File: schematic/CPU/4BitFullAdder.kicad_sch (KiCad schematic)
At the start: 5 parts, among them U23 74LS86, U24 74LS08, U25 74LS86, U26 74LS08, U27 74LS32

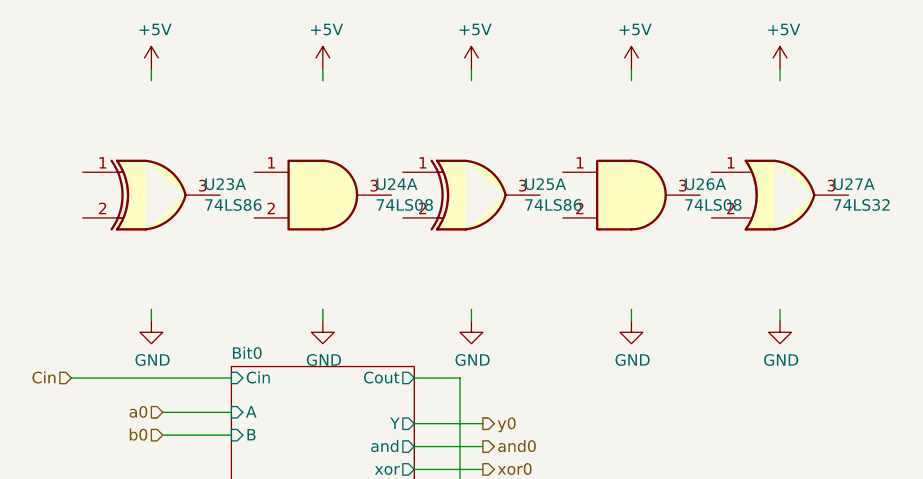
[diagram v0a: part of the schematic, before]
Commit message: ttl fpga: factorization works in sim and fpga
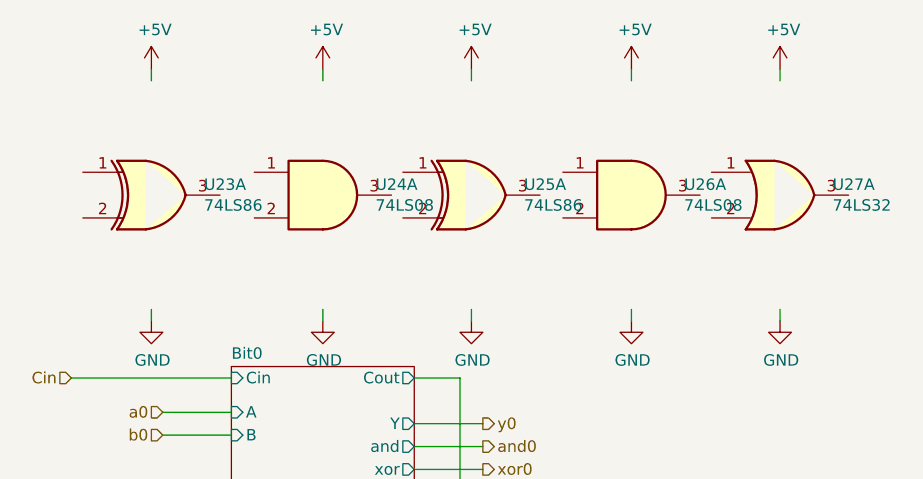
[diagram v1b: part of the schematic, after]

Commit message: io: async register + reversed bus
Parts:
- renumbered U23 to U28, U24 to U29, U25 to U30, U26 to U31, U27 to U32
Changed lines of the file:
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@@
   (symbol (lib_id "74xx:74LS86") (at 73.66 39.37 0)
     (in_bom yes) (on_board yes)
-    (property "Reference" "U23" (id 0) (at 79.502 38.2016 0)
+    (property "Reference" "U28" (id 0) (at 79.502 38.2016 0)
       (effects (font (size 1.27 1.27)) (justify left))
     )
@@
   (symbol (lib_id "74xx:74LS86") (at 109.22 39.37 0)
     (in_bom yes) (on_board yes)
-    (property "Reference" "U25" (id 0) (at 115.062 38.2016 0)
+    (property "Reference" "U30" (id 0) (at 115.062 38.2016 0)
       (effects (font (size 1.27 1.27)) (justify left))
     )
@@
   (symbol (lib_id "74xx:74LS08") (at 92.71 39.37 0)
     (in_bom yes) (on_board yes)
-    (property "Reference" "U24" (id 0) (at 98.552 38.2016 0)
+    (property "Reference" "U29" (id 0) (at 98.552 38.2016 0)
       (effects (font (size 1.27 1.27)) (justify left))
     )
@@
   (symbol (lib_id "74xx:74LS08") (at 127 39.37 0)
     (in_bom yes) (on_board yes)
-    (property "Reference" "U26" (id 0) (at 132.842 38.2016 0)
+    (property "Reference" "U31" (id 0) (at 132.842 38.2016 0)
       (effects (font (size 1.27 1.27)) (justify left))
     )
@@
   (symbol (lib_id "74xx:74LS32") (at 143.51 39.37 0)
     (in_bom yes) (on_board yes)
-    (property "Reference" "U27" (id 0) (at 149.352 38.2016 0)
+    (property "Reference" "U32" (id 0) (at 149.352 38.2016 0)
       (effects (font (size 1.27 1.27)) (justify left))
     )
@@
   (symbol (lib_id "power:+5V") (at 73.66 25.4 0)
     (in_bom yes) (on_board yes)
-    (property "Reference" "#PWR081" (id 0) (at 73.66 29.21 0)
+    (property "Reference" "#PWR091" (id 0) (at 73.66 29.21 0)
       (effects (font (size 1.27 1.27)) hide)
     )
@@
   (symbol (lib_id "power:+5V") (at 92.71 25.4 0)
     (in_bom yes) (on_board yes)
-    (property "Reference" "#PWR083" (id 0) (at 92.71 29.21 0)
+    (property "Reference" "#PWR093" (id 0) (at 92.71 29.21 0)
       (effects (font (size 1.27 1.27)) hide)
     )
@@
   (symbol (lib_id "power:+5V") (at 109.22 25.4 0)
     (in_bom yes) (on_board yes)
-    (property "Reference" "#PWR085" (id 0) (at 109.22 29.21 0)
+    (property "Reference" "#PWR095" (id 0) (at 109.22 29.21 0)
       (effects (font (size 1.27 1.27)) hide)
     )
@@
   (symbol (lib_id "power:GND") (at 143.51 53.34 0)
     (in_bom yes) (on_board yes)
-    (property "Reference" "#PWR090" (id 0) (at 143.51 59.69 0)
+    (property "Reference" "#PWR0100" (id 0) (at 143.51 59.69 0)
       (effects (font (size 1.27 1.27)) hide)
     )
@@
   (symbol (lib_id "power:GND") (at 127 53.34 0)
     (in_bom yes) (on_board yes)
-    (property "Reference" "#PWR088" (id 0) (at 127 59.69 0)
+    (property "Reference" "#PWR098" (id 0) (at 127 59.69 0)
       (effects (font (size 1.27 1.27)) hide)
     )
@@
   (symbol (lib_id "power:GND") (at 109.22 53.34 0)
     (in_bom yes) (on_board yes)
-    (property "Reference" "#PWR086" (id 0) (at 109.22 59.69 0)
+    (property "Reference" "#PWR096" (id 0) (at 109.22 59.69 0)
       (effects (font (size 1.27 1.27)) hide)
     )
@@
   (symbol (lib_id "power:GND") (at 92.71 53.34 0)
     (in_bom yes) (on_board yes)
-    (property "Reference" "#PWR084" (id 0) (at 92.71 59.69 0)
+    (property "Reference" "#PWR094" (id 0) (at 92.71 59.69 0)
       (effects (font (size 1.27 1.27)) hide)
     )
@@
   (symbol (lib_id "power:GND") (at 73.66 53.34 0)
     (in_bom yes) (on_board yes)
-    (property "Reference" "#PWR082" (id 0) (at 73.66 59.69 0)
+    (property "Reference" "#PWR092" (id 0) (at 73.66 59.69 0)
       (effects (font (size 1.27 1.27)) hide)
     )
@@
   (symbol (lib_id "power:+5V") (at 127 25.4 0)
     (in_bom yes) (on_board yes)
-    (property "Reference" "#PWR087" (id 0) (at 127 29.21 0)
+    (property "Reference" "#PWR097" (id 0) (at 127 29.21 0)
       (effects (font (size 1.27 1.27)) hide)
     )
@@
   (symbol (lib_id "power:+5V") (at 143.51 25.4 0)
     (in_bom yes) (on_board yes)
-    (property "Reference" "#PWR089" (id 0) (at 143.51 29.21 0)
-      (effects (font (size 1.27 1.27)) hide)
-    )
+    (property "Reference" "#PWR099" (id 0) (at 143.51 29.21 0)
+      (effects (font (size 1.27 1.27)) hide)
+    )

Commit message: alu figures, modules finished
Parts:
- U28, U30: value 74LS86 -> (none); footprint Package_DIP:DIP-14_W7.62mm -> (none)
- U29, U31: value 74LS08 -> (none); footprint Package_DIP:DIP-14_W7.62mm -> (none)
- U32: value 74LS32 -> (none); footprint Package_DIP:DIP-14_W7.62mm -> (none)
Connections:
- net +5V: now also U28.14 (VCC), U29.14 (VCC), U30.14 (VCC), U31.14 (VCC), U32.14 (VCC)
- net GND: now also U28.7 (GND), U29.7 (GND), U30.7 (GND), U31.7 (GND), U32.7 (GND)
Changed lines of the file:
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@@
     (effects (font (size 1.27 1.27)) (justify right))
   )
-  (symbol (lib_id "74xx:74LS86") (at 73.66 39.37 0)
+  (symbol (lib_id "74xx:74LS86") (at 73.66 39.37 0) (unit 5)
     (in_bom yes) (on_board yes)
     (property "Reference" "U28" (id 0) (at 79.502 38.2016 0)
       (effects (font (size 1.27 1.27)) (justify left))
     )
-    (property "Value" "74LS86" (id 1) (at 79.502 40.513 0)
-      (effects (font (size 1.27 1.27)) (justify left))
-    )
-    (property "Footprint" "Package_DIP:DIP-14_W7.62mm" (id 2) (at 73.66 39.37 0)
+    (property "Value" "" (id 1) (at 79.502 40.513 0)
+      (effects (font (size 1.27 1.27)) (justify left))
+    )
+    (property "Footprint" "" (id 2) (at 73.66 39.37 0)
       (effects (font (size 1.27 1.27)) hide)
     )
@@
       (effects (font (size 1.27 1.27)) hide)
     )
-    (pin "14")
-    (pin "7")
-  )
-  (symbol (lib_id "74xx:74LS86") (at 109.22 39.37 0)
+    (pin "1")
+    (pin "2")
+    (pin "3")
+    (pin "4")
+    (pin "5")
+    (pin "6")
+    (pin "10")
+    (pin "8")
+    (pin "9")
+    (pin "11")
+    (pin "12")
+    (pin "13")
+    (pin "14")
+    (pin "7")
+  )
+  (symbol (lib_id "74xx:74LS86") (at 109.22 39.37 0) (unit 5)
     (in_bom yes) (on_board yes)
     (property "Reference" "U30" (id 0) (at 115.062 38.2016 0)
       (effects (font (size 1.27 1.27)) (justify left))
     )
-    (property "Value" "74LS86" (id 1) (at 115.062 40.513 0)
-      (effects (font (size 1.27 1.27)) (justify left))
-    )
-    (property "Footprint" "Package_DIP:DIP-14_W7.62mm" (id 2) (at 109.22 39.37 0)
+    (property "Value" "" (id 1) (at 115.062 40.513 0)
+      (effects (font (size 1.27 1.27)) (justify left))
+    )
+    (property "Footprint" "" (id 2) (at 109.22 39.37 0)
       (effects (font (size 1.27 1.27)) hide)
     )
@@
       (effects (font (size 1.27 1.27)) hide)
     )
-    (pin "14")
-    (pin "7")
-  )
-  (symbol (lib_id "74xx:74LS08") (at 92.71 39.37 0)
+    (pin "1")
+    (pin "2")
+    (pin "3")
+    (pin "4")
+    (pin "5")
+    (pin "6")
+    (pin "10")
+    (pin "8")
+    (pin "9")
+    (pin "11")
+    (pin "12")
+    (pin "13")
+    (pin "14")
+    (pin "7")
+  )
+  (symbol (lib_id "74xx:74LS08") (at 92.71 39.37 0) (unit 5)
     (in_bom yes) (on_board yes)
     (property "Reference" "U29" (id 0) (at 98.552 38.2016 0)
       (effects (font (size 1.27 1.27)) (justify left))
     )
-    (property "Value" "74LS08" (id 1) (at 98.552 40.513 0)
-      (effects (font (size 1.27 1.27)) (justify left))
-    )
-    (property "Footprint" "Package_DIP:DIP-14_W7.62mm" (id 2) (at 92.71 39.37 0)
+    (property "Value" "" (id 1) (at 98.552 40.513 0)
+      (effects (font (size 1.27 1.27)) (justify left))
+    )
+    (property "Footprint" "" (id 2) (at 92.71 39.37 0)
       (effects (font (size 1.27 1.27)) hide)
     )
@@
       (effects (font (size 1.27 1.27)) hide)
     )
-    (pin "14")
-    (pin "7")
-  )
-  (symbol (lib_id "74xx:74LS08") (at 127 39.37 0)
+    (pin "1")
+    (pin "2")
+    (pin "3")
+    (pin "4")
+    (pin "5")
+    (pin "6")
+    (pin "10")
+    (pin "8")
+    (pin "9")
+    (pin "11")
+    (pin "12")
+    (pin "13")
+    (pin "14")
+    (pin "7")
+  )
+  (symbol (lib_id "74xx:74LS08") (at 127 39.37 0) (unit 5)
     (in_bom yes) (on_board yes)
     (property "Reference" "U31" (id 0) (at 132.842 38.2016 0)
       (effects (font (size 1.27 1.27)) (justify left))
     )
-    (property "Value" "74LS08" (id 1) (at 132.842 40.513 0)
-      (effects (font (size 1.27 1.27)) (justify left))
-    )
-    (property "Footprint" "Package_DIP:DIP-14_W7.62mm" (id 2) (at 127 39.37 0)
+    (property "Value" "" (id 1) (at 132.842 40.513 0)
+      (effects (font (size 1.27 1.27)) (justify left))
+    )
+    (property "Footprint" "" (id 2) (at 127 39.37 0)
       (effects (font (size 1.27 1.27)) hide)
     )
@@
       (effects (font (size 1.27 1.27)) hide)
     )
-    (pin "14")
-    (pin "7")
-  )
-  (symbol (lib_id "74xx:74LS32") (at 143.51 39.37 0)
+    (pin "1")
+    (pin "2")
+    (pin "3")
+    (pin "4")
+    (pin "5")
+    (pin "6")
+    (pin "10")
+    (pin "8")
+    (pin "9")
+    (pin "11")
+    (pin "12")
+    (pin "13")
+    (pin "14")
+    (pin "7")
+  )
+  (symbol (lib_id "74xx:74LS32") (at 143.51 39.37 0) (unit 5)
     (in_bom yes) (on_board yes)
     (property "Reference" "U32" (id 0) (at 149.352 38.2016 0)
       (effects (font (size 1.27 1.27)) (justify left))
     )
-    (property "Value" "74LS32" (id 1) (at 149.352 40.513 0)
-      (effects (font (size 1.27 1.27)) (justify left))
-    )
-    (property "Footprint" "Package_DIP:DIP-14_W7.62mm" (id 2) (at 143.51 39.37 0)
+    (property "Value" "" (id 1) (at 149.352 40.513 0)
+      (effects (font (size 1.27 1.27)) (justify left))
+    )
+    (property "Footprint" "" (id 2) (at 143.51 39.37 0)
       (effects (font (size 1.27 1.27)) hide)
     )
@@
       (effects (font (size 1.27 1.27)) hide)
     )
-    (pin "14")
-    (pin "7")
-  )
-  (symbol (lib_id "power:+5V") (at 73.66 25.4 0)
-    (in_bom yes) (on_board yes)
-    (property "Reference" "#PWR081" (id 0) (at 73.66 29.21 0)
+    (pin "1")
+    (pin "2")
+    (pin "3")
+    (pin "4")
+    (pin "5")
+    (pin "6")
+    (pin "10")
+    (pin "8")
+    (pin "9")
+    (pin "11")
+    (pin "12")
+    (pin "13")
+    (pin "14")
+    (pin "7")
+  )
+  (symbol (lib_id "power:+5V") (at 73.66 25.4 0) (unit 1)
+    (in_bom yes) (on_board yes)
+    (property "Reference" "#PWR091" (id 0) (at 73.66 29.21 0)
       (effects (font (size 1.27 1.27)) hide)
     )
@@
     (pin "1")
   )
-  (symbol (lib_id "power:+5V") (at 92.71 25.4 0)
-    (in_bom yes) (on_board yes)
-    (property "Reference" "#PWR083" (id 0) (at 92.71 29.21 0)
+  (symbol (lib_id "power:+5V") (at 92.71 25.4 0) (unit 1)
+    (in_bom yes) (on_board yes)
+    (property "Reference" "#PWR093" (id 0) (at 92.71 29.21 0)
       (effects (font (size 1.27 1.27)) hide)
     )
@@
     (pin "1")
   )
-  (symbol (lib_id "power:+5V") (at 109.22 25.4 0)
-    (in_bom yes) (on_board yes)
-    (property "Reference" "#PWR085" (id 0) (at 109.22 29.21 0)
+  (symbol (lib_id "power:+5V") (at 109.22 25.4 0) (unit 1)
+    (in_bom yes) (on_board yes)
+    (property "Reference" "#PWR095" (id 0) (at 109.22 29.21 0)
       (effects (font (size 1.27 1.27)) hide)
     )
@@
     (pin "1")
   )
-  (symbol (lib_id "power:GND") (at 143.51 53.34 0)
-    (in_bom yes) (on_board yes)
-    (property "Reference" "#PWR090" (id 0) (at 143.51 59.69 0)
+  (symbol (lib_id "power:GND") (at 143.51 53.34 0) (unit 1)
+    (in_bom yes) (on_board yes)
+    (property "Reference" "#PWR0100" (id 0) (at 143.51 59.69 0)
       (effects (font (size 1.27 1.27)) hide)
     )
@@
     (pin "1")
   )
-  (symbol (lib_id "power:GND") (at 127 53.34 0)
-    (in_bom yes) (on_board yes)
-    (property "Reference" "#PWR088" (id 0) (at 127 59.69 0)
+  (symbol (lib_id "power:GND") (at 127 53.34 0) (unit 1)
+    (in_bom yes) (on_board yes)
+    (property "Reference" "#PWR098" (id 0) (at 127 59.69 0)
       (effects (font (size 1.27 1.27)) hide)
     )
@@
     (pin "1")
   )
-  (symbol (lib_id "power:GND") (at 109.22 53.34 0)
-    (in_bom yes) (on_board yes)
-    (property "Reference" "#PWR086" (id 0) (at 109.22 59.69 0)
+  (symbol (lib_id "power:GND") (at 109.22 53.34 0) (unit 1)
+    (in_bom yes) (on_board yes)
+    (property "Reference" "#PWR096" (id 0) (at 109.22 59.69 0)
       (effects (font (size 1.27 1.27)) hide)
     )
@@
     (pin "1")
   )
-  (symbol (lib_id "power:GND") (at 92.71 53.34 0)
-    (in_bom yes) (on_board yes)
-    (property "Reference" "#PWR084" (id 0) (at 92.71 59.69 0)
+  (symbol (lib_id "power:GND") (at 92.71 53.34 0) (unit 1)
+    (in_bom yes) (on_board yes)
+    (property "Reference" "#PWR094" (id 0) (at 92.71 59.69 0)
       (effects (font (size 1.27 1.27)) hide)
     )
@@
     (pin "1")
   )
-  (symbol (lib_id "power:GND") (at 73.66 53.34 0)
-    (in_bom yes) (on_board yes)
-    (property "Reference" "#PWR082" (id 0) (at 73.66 59.69 0)
+  (symbol (lib_id "power:GND") (at 73.66 53.34 0) (unit 1)
+    (in_bom yes) (on_board yes)
+    (property "Reference" "#PWR092" (id 0) (at 73.66 59.69 0)
       (effects (font (size 1.27 1.27)) hide)
     )
@@
     (pin "1")
   )
-  (symbol (lib_id "power:+5V") (at 127 25.4 0)
-    (in_bom yes) (on_board yes)
-    (property "Reference" "#PWR087" (id 0) (at 127 29.21 0)
+  (symbol (lib_id "power:+5V") (at 127 25.4 0) (unit 1)
+    (in_bom yes) (on_board yes)
+    (property "Reference" "#PWR097" (id 0) (at 127 29.21 0)
       (effects (font (size 1.27 1.27)) hide)
     )
@@
     (pin "1")
   )
-  (symbol (lib_id "power:+5V") (at 143.51 25.4 0)
-    (in_bom yes) (on_board yes)
-    (property "Reference" "#PWR089" (id 0) (at 143.51 29.21 0)
-      (effects (font (size 1.27 1.27)) hide)
-    )
+  (symbol (lib_id "power:+5V") (at 143.51 25.4 0) (unit 1)
+    (in_bom yes) (on_board yes)
+    (property "Reference" "#PWR099" (id 0) (at 143.51 29.21 0)
+      (effects (font (size 1.27 1.27)) hide)
+    )
